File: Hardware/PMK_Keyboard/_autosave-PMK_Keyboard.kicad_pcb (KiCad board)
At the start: 2 copper layers, 152 x 134.8 mm, 62 parts, among them IC1 SN74HC165PWR, IC2 SN74HC165PWR, IC3 SN74HC165PWR, IC4 SN74HC165PWR, IC5 SN74HC165PWR, IC6 SN74HC165PWR, IC7 ESP32-S2FH4, SW1 SW_Push, SW10 SW_Push, SW11 SW_Push, SW12 SW_Push, SW13 SW_Push, SW14 SW_Push, SW15 SW_Push, SW16 SW_Push, SW17 SW_Push, SW18 SW_Push, SW19 SW_Push, SW2 SW_Push, SW20 SW_Push, SW21 SW_Push, SW22 SW_Push, SW23 SW_Push, SW24 SW_Push, SW25 SW_Push, SW26 SW_Push, SW27 SW_Push, SW28 SW_Push, SW29 SW_Push, SW3 SW_Push, SW30 SW_Push, SW31 SW_Push, SW32 SW_Push, SW33 SW_Push, SW34 SW_Push, SW35 SW_Push, SW36 SW_Push, SW37 SW_Push, SW38 SW_Push, SW39 SW_Push, SW4 SW_Push, SW40 SW_Push, SW41 SW_Push, SW42 SW_Push, SW43 SW_Push, SW44 SW_Push, SW45 SW_Push, SW46 SW_Push, SW47 SW_Push, SW48 SW_Push, SW5 SW_Push, SW6 SW_Push, SW7 SW_Push, SW8 SW_Push, SW9 SW_Push

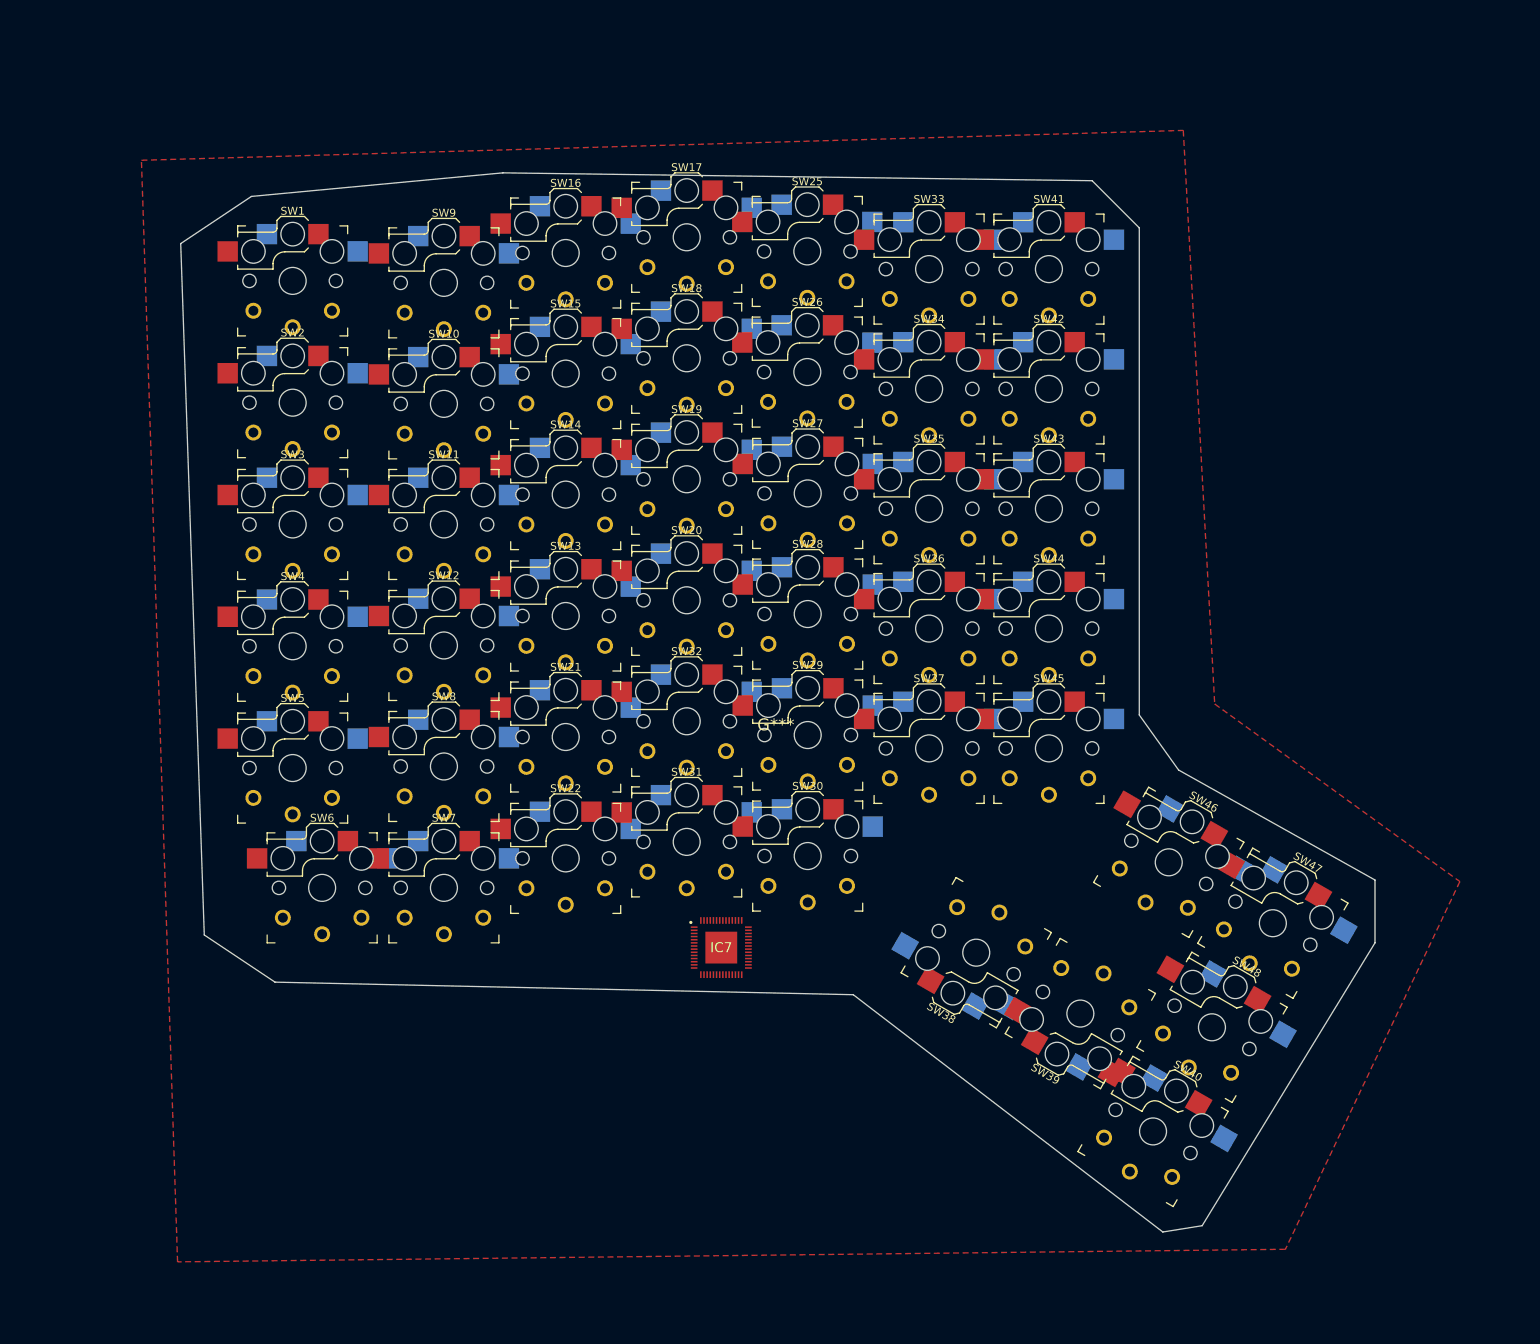
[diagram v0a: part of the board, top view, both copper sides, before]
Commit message: finally the correct pcb dimension
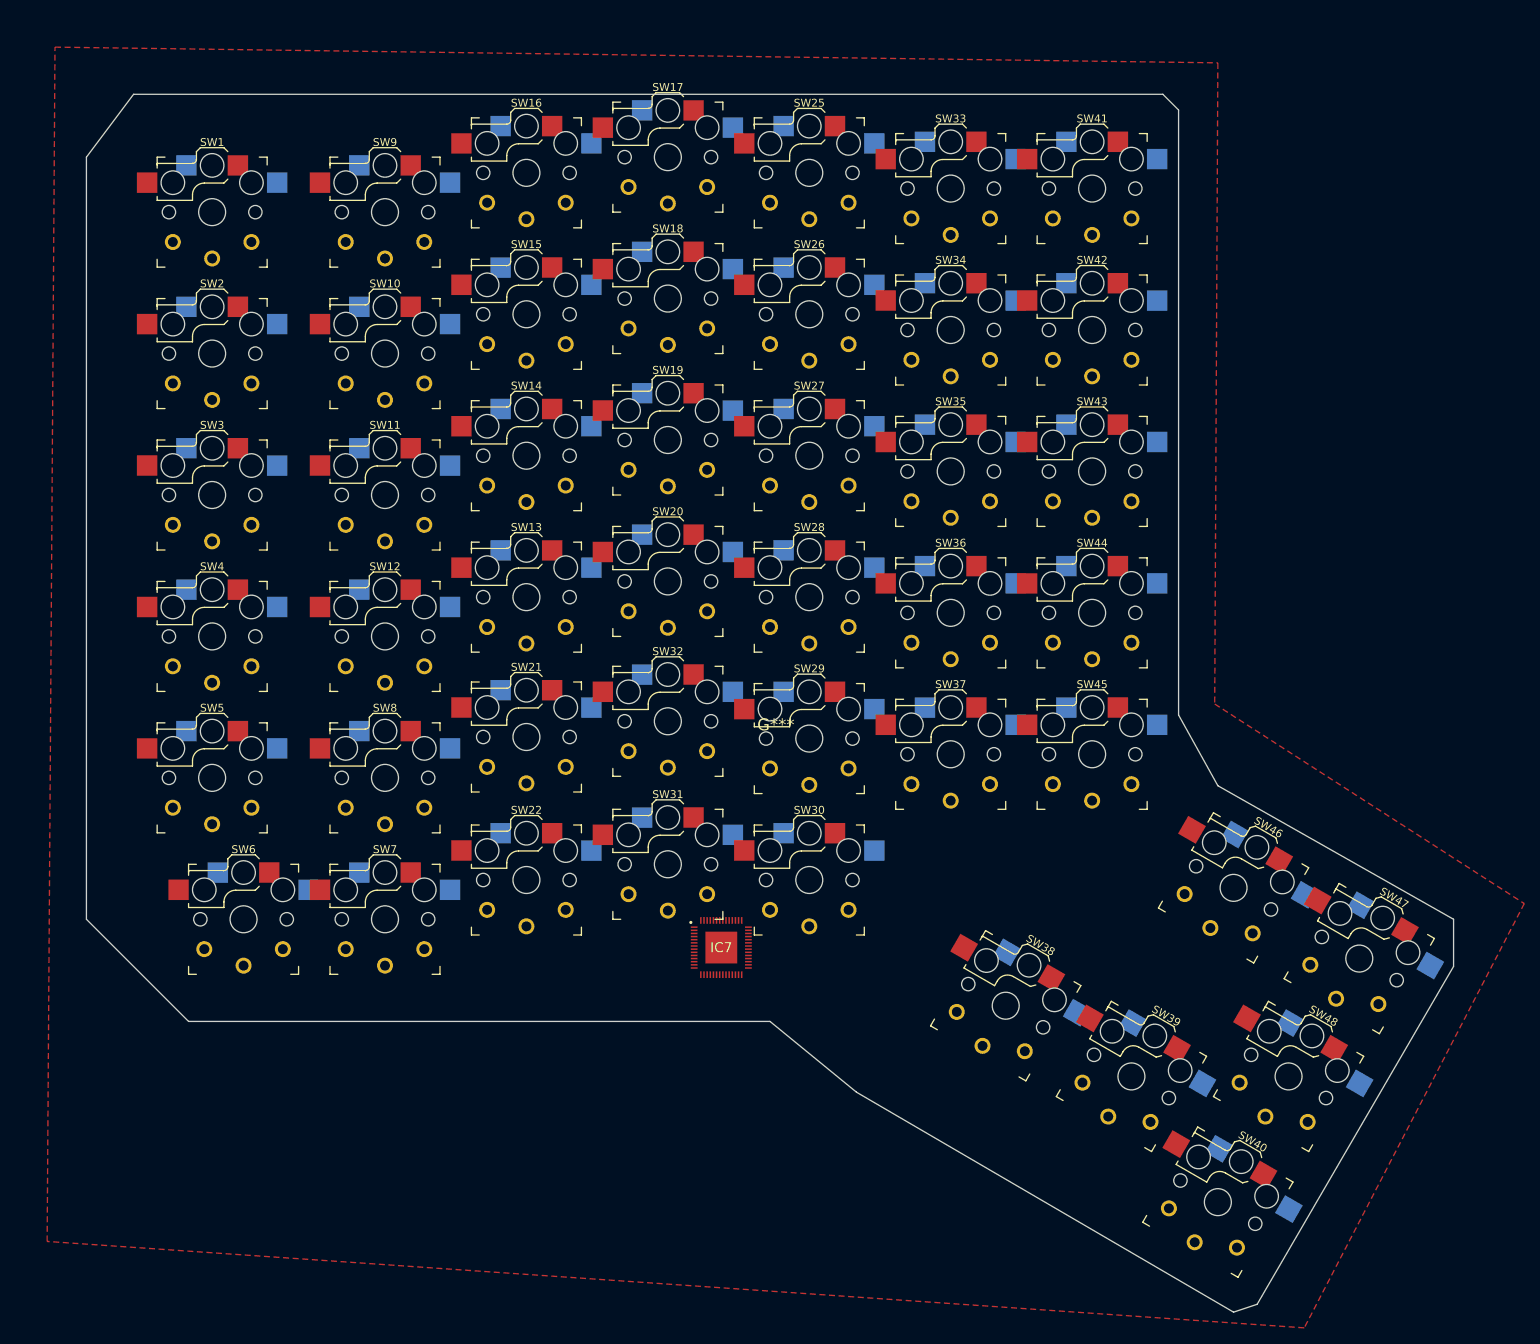
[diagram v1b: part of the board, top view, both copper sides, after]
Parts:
- moved SW1 13.5 mm to (32.0, 57.0)
- moved SW40 12.2 mm to (160.0, 183.0)
- moved SW2 12.0 mm to (32.0, 75.0)
- moved SW47 11.9 mm to (178.0, 152.0)
- moved SW9 11.7 mm to (54.0, 57.0)
- moved SW41 11.6 mm to (144.0, 54.0)
- moved SW48 11.6 mm to (169.0, 167.0)
- moved SW16 11.4 mm to (72.0, 52.0)
- moved SW3 10.9 mm to (32.0, 93.0)
- moved SW6 10.8 mm to (36.0, 147.0)
- moved SW33 10.6 mm to (126.0, 54.0)
- moved SW17 10.5 mm to (90.0, 50.0)
- moved SW4 10.3 mm to (32.0, 111.0)
- moved SW5 10.3 mm to (32.0, 129.0)
- moved SW39 10.3 mm to (149.0, 167.0), turned to -30 degrees
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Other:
- board size 152 x 134.8 mm -> 174 x 155 mm
